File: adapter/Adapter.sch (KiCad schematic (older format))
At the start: 51 parts, among them J1 USB_B_Micro, J2 2040210-1, J3 USB_C_Receptacle, J4 Conn_01x05_Male, J5 Conn_01x03_Male, Q1 IRLML2244TRPBF, SW1 RESET, SW2 BOOT, U1 SN75DP119, U2 AZ1117-3.3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

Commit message: state published at http://strfry.org/lg360vr-schematic.pdf
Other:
- note added: "Design Considerations.\n\nWhat to do with extra lane on DP redriver?\n -> route DP1+- as well, disable lane through EN-Z in software\n-> dont route, save hassle, focus on matching DP0\n\nTerminate extra DP lanes or leave open? \n-> just leave as is, link training should disable them\n\n\nMake use of USB in STM32?-> Break out to pin headers?\n-> maybe, just maybe: connect to device USB, and leave 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"
- note added: "STM32 Q&A:\nDoes the VBAT need to be connected? yes, to VDD\nDo we need special decoupling for AVDD? yes, preferably doucupled with bead.\nTODO: Use reference bead\n\nWhich are the analog pins?\nstm32f072rb.pdf p.33 ff -> PA0-PA7, PB0-1\n\n\n5V Tolerant pins?\n-> PF0-1, PB10-11\nTODO: Make sure LED pins are 5V tolerant\n\n\nHow to do reset? -> can it be left floating / on SWD connector?\n-> pulld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"
- note added: "TODO: Compute Resistors\n"
- note added: "Try to do AUX-Snooping..."
- note removed: "AC coupling on RX side?\n\nWhich type of couple cap?"
- note removed: "Compute Resistors\n"
- note removed: "Design Considerations.\n\nWhat to do with extra lane on DP redriver?\n -> route DP1+- as well, disable lane through EN-Z in software\n-> dont route, save hassle, focus on matching DP0\n\nTerminate extra DP lanes or leave open? \n\n\nMake use of USB in STM32?-> Break out to pin headers?\n-> maybe, just maybe: connect to device USB, and leave floating?\n\n\nConnect CONFIG1/CONFIG2 to microcontrolle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"
- note removed: "STM32 Q&A:\nDoes the VBAT need to be connected? yes, to VDD\nDo we need special decoupling for AVDD? yes, with bead\n\nWhich are the analog pins?\nstm32f072rb.pdf p.33 ff -> PA0-PA7, PB0-1\n\n\n5V Tolerant pins?\n-> PF0-1, PB10-11\n\n\nHow to do reset? -> can it be left floating / on SWD connector?\n\n\nWhat is BOOT0?\n\n\nHow we do programming? -> expose SWD Pins + VDD + RESET\n\nDo PF0/1 have a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"
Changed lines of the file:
@@
 encoding utf-8
 Sheet 1 1
-Title ""
-Date ""
-Rev ""
-Comp ""
-Comment1 ""
+Title "LG360VR Adapter Board"
+Date "2019-02-06"
+Rev "v1"
+Comp "strfry"
+Comment1 "Draft"
 Comment2 ""
 Comment3 ""
@@
 	1    0    0    -1
 $EndComp
-Text Notes -2250 7250 0    50   ~ 0
-STM32 Q&A:\nDoes the VBAT need to be connected? yes, to VDD\nDo we need special decoupling for AVDD? yes, with bead\n\nWhich are the analog pins?\nstm32f072rb.pdf p.33 ff -> PA0-PA7, PB0-1\n\n\n5V Tolerant pins?\n-> PF0-1, PB10-11\n\n\nHow to do reset?  -> can it be left floating / on SWD connector?\n\n\nWhat is BOOT0?\n\n\nHow we do programming? -> expose SWD Pins + VDD + RESET\n\nDo PF0/1 have a special function? -> Yes, the Mhz Quartz\n\nOpt to not populate Crystal? F0x2 is "crystalless USB type"
-Text Notes -3950 4750 0    50   ~ 0
-Design Considerations.\n\nWhat to do with extra lane on DP redriver?\n -> route DP1+- as well, disable lane through EN-Z in software\n-> dont route, save hassle, focus on matching DP0\n\nTerminate extra DP lanes or leave open? \n\n\nMake use of USB in STM32?-> Break out to pin headers?\n-> maybe, just maybe: connect to device USB, and leave floating?\n\n\nConnect CONFIG1/CONFIG2 to microcontroller, just in case? -> Connect CONFIG2 to CEC AF-Pin\n-> CONFIG1/CONFIG2 is not I2C, would need separate conn to AUX: \nhttp://mikesmods.com/mm-wp/wp-content/uploads/2014/03/Commercial_DP2DVI_Adapter.pdf\n\n\nShould USB-C VBUS be FET switchable? Should CC lines be switched as well?\n-> TI Paper says Disconnect FET is needed -> sth. like \nHigh Side PMOS: IRLML2244TRPBF\n\n\nUSB-PD CC PHY?\n\n\nSPI Self Clock!!!\n
+Text Notes -3000 7450 0    50   ~ 0
+STM32 Q&A:\nDoes the VBAT need to be connected? yes, to VDD\nDo we need special decoupling for AVDD? yes, preferably doucupled with bead.\nTODO: Use reference bead\n\nWhich are the analog pins?\nstm32f072rb.pdf p.33 ff -> PA0-PA7, PB0-1\n\n\n5V Tolerant pins?\n-> PF0-1, PB10-11\nTODO: Make sure LED pins are 5V tolerant\n\n\nHow to do reset?  -> can it be left floating / on SWD connector?\n-> pulldown and provide button\n\nWhat is BOOT0?\n-> essentially enables builtin serial bootrom, unless disabled by config register\n\n\nHow we do programming? -> expose SWD Pins + VDD + RESET\n\nDo PF0/1 have a special function? -> Yes, the Mhz Quartz\n\nOpt to not populate Crystal? F0x2 is "crystalless USB type"
+Text Notes -3850 3250 0    50   ~ 0
+Design Considerations.\n\nWhat to do with extra lane on DP redriver?\n -> route DP1+- as well, disable lane through EN-Z in software\n-> dont route, save hassle, focus on matching DP0\n\nTerminate extra DP lanes or leave open? \n-> just leave as is, link training should disable them\n\n\nMake use of USB in STM32?-> Break out to pin headers?\n-> maybe, just maybe: connect to device USB, and leave floating?\n\n\nConnect CONFIG1/CONFIG2 to microcontroller, just in case? -> Connect CONFIG2 to CEC AF-Pin\n-> CONFIG1/CONFIG2 is not I2C, would need separate conn to AUX: \nhttp://mikesmods.com/mm-wp/wp-content/uploads/2014/03/Commercial_DP2DVI_Adapter.pdf\n-> dont bother\n\nShould USB-C VBUS be FET switchable? Should CC lines be switched as well?\n-> TI Paper says Disconnect FET is needed -> sth. like \nHigh Side PMOS: IRLML2244TRPBF\n\n\nUSB-PD CC PHY? -> almost done\nTODO: Correct resistor value for 3.3V\n\n\nSPI Self Clock!!! -> check, TX_CLK\n\n\nAC coupling on RX side? -> yes\n\nWhich type of couple cap?\n-> Intel doc on PCIe recommend 100nF X7R, should be fine
 NoConn ~ 5000 1600
 NoConn ~ 5000 1700
@@
 	1    0    0    -1
 $EndComp
-Text Notes 6750 1100 0    50   ~ 0
-AC coupling on RX side?\n\nWhich type of couple cap?
 $Comp
 L power:VDD #PWR0123
@@
 Discuss best connector type
 Text Notes 850  7550 0    50   ~ 0
-Compute Resistors\n
+TODO: Compute Resistors\n
+Text Notes 4050 6150 0    50   ~ 0
+Try to do AUX-Snooping...
 $EndSCHEMATC

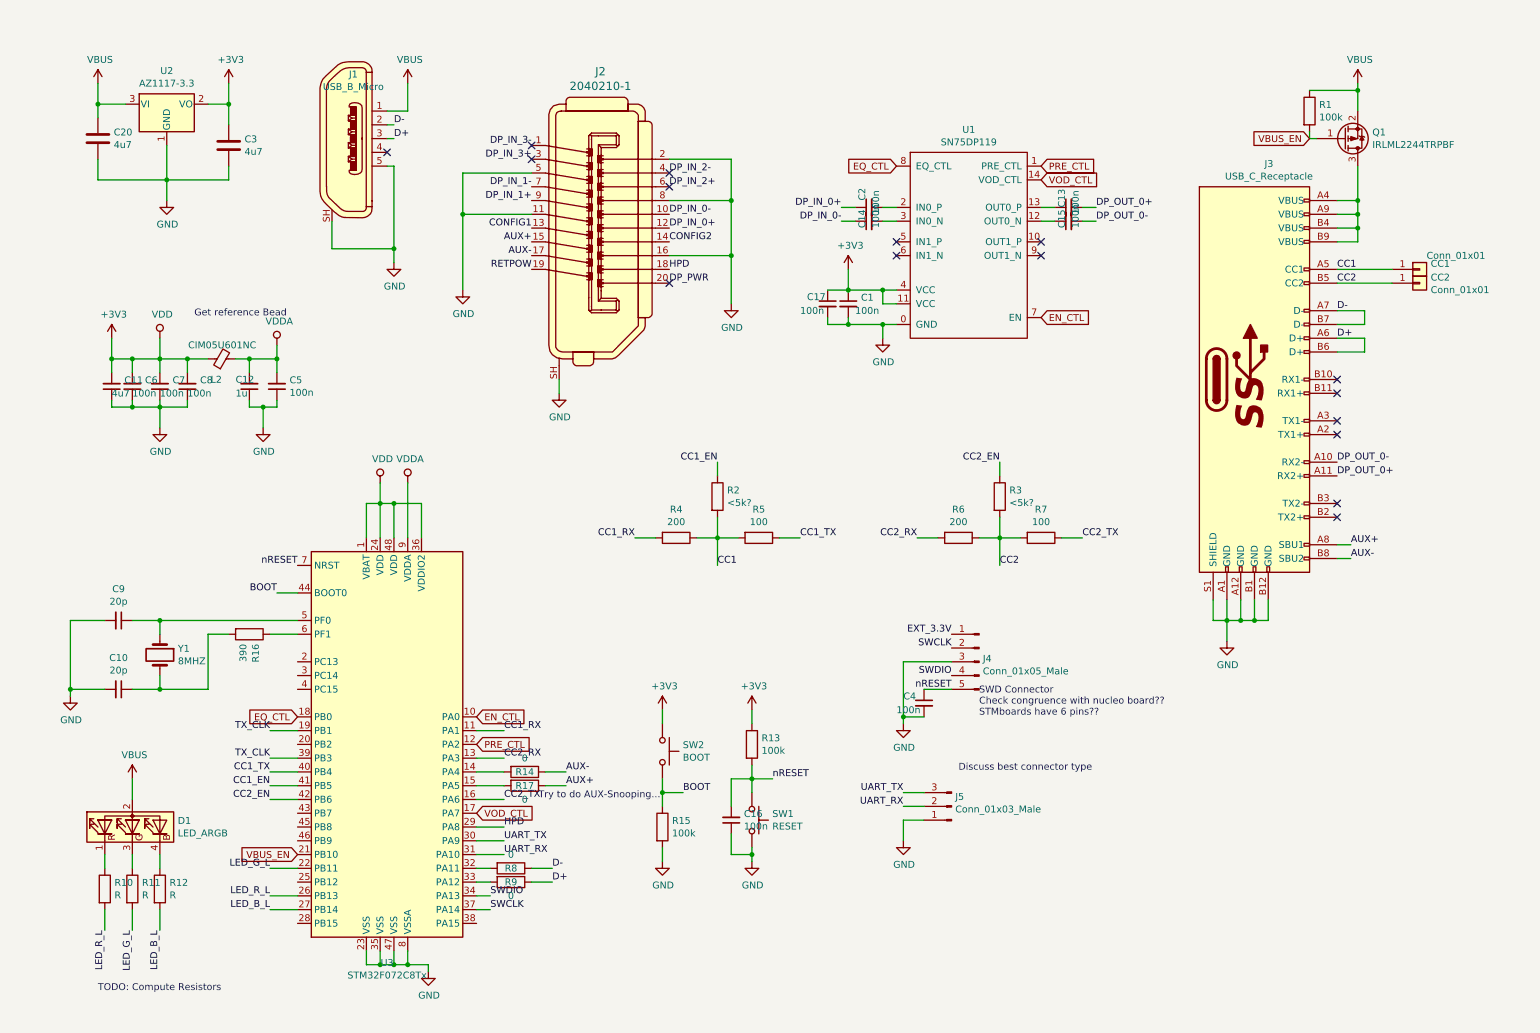
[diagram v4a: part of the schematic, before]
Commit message: Replaced SN75DP119 symbol/footprint with premade one from Arrow librarian
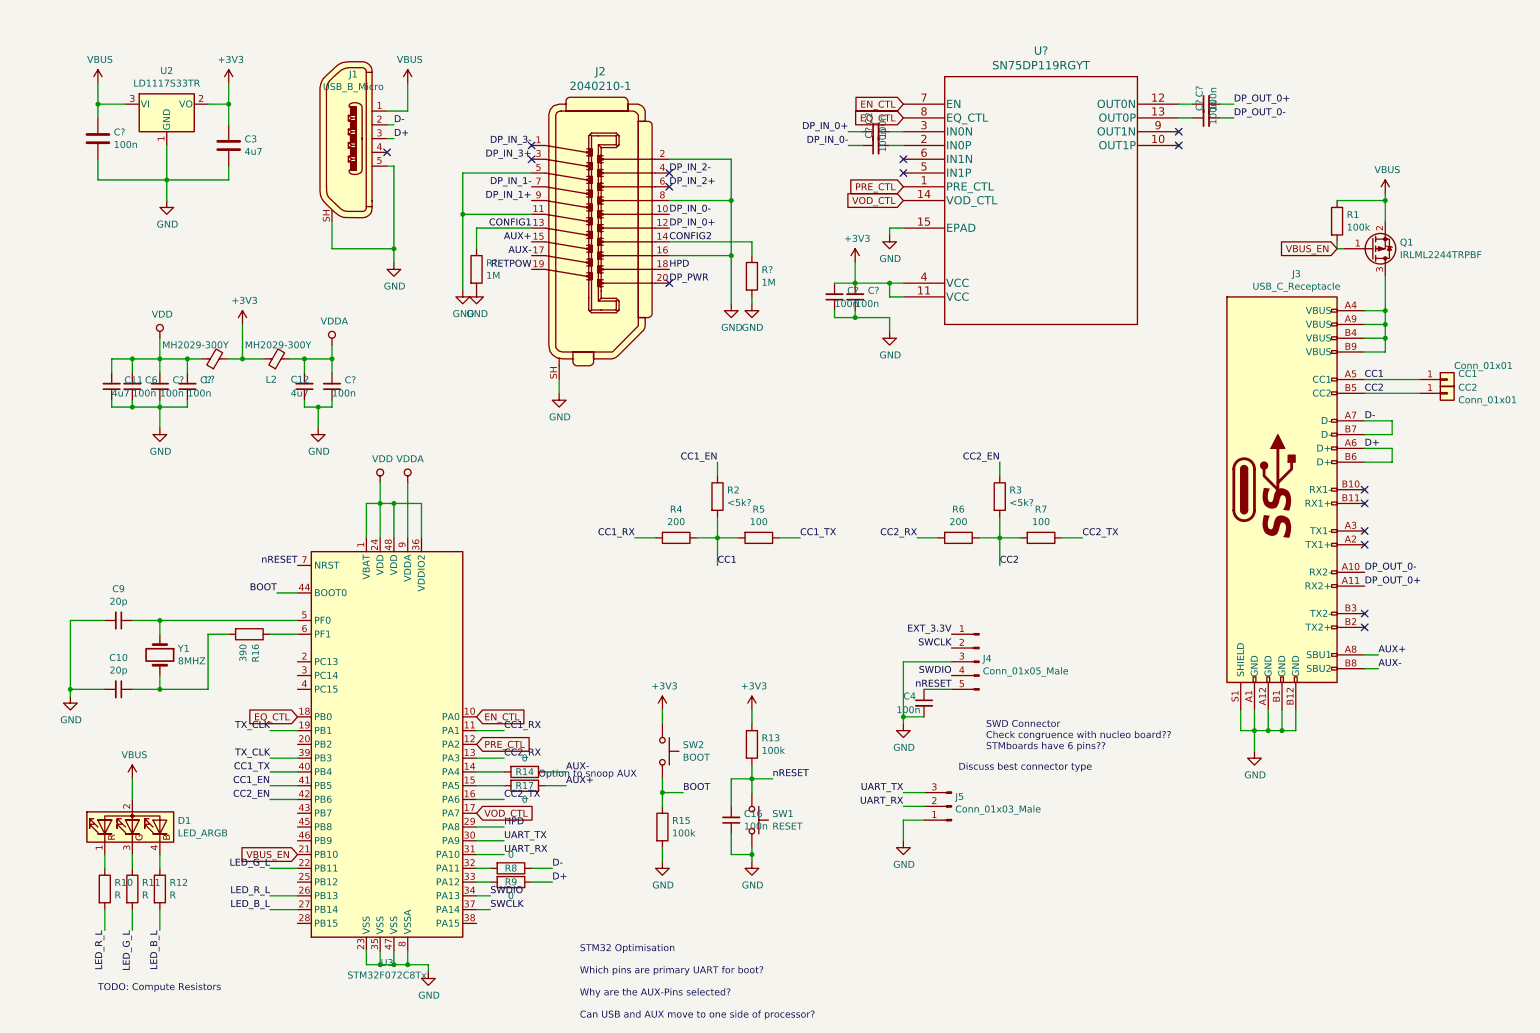
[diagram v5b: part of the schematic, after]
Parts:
- removed C1, C17, C5, C7, C8: 100n, Capacitor_SMD:C_0603_1608Metric_Pad1.05x0.95mm_HandSolder, symbol Device:C_Small
- removed C13, C14, C15: 100n, Capacitor_SMD:C_0402_1005Metric, symbol Device:C_Small
- removed C20: 4u7, Capacitor_SMD:C_0603_1608Metric_Pad1.05x0.95mm_HandSolder, symbol Device:C
- removed U1: SN75DP119, SN75DP119:QFN-20-1EP_4x4mm_P0.5mm_EP2.5x2.5mm, symbol DisplayPort_Redriver:SN75DP119
- added C?: 100n, Capacitor_SMD:C_0603_1608Metric_Pad1.05x0.95mm_HandSolder, symbol Device:C
- added C? (x5): 100n, Capacitor_SMD:C_0603_1608Metric_Pad1.05x0.95mm_HandSolder, symbol Device:C_Small
- added C? (x3): 100n, Capacitor_SMD:C_0402_1005Metric, symbol Device:C_Small
- added L?: MH2029-300Y, Inductor_SMD:L_0805_2012Metric_Pad1.15x1.40mm_HandSolder, symbol Device:Ferrite_Bead_Small
- added R? (x2): 1M, symbol Device:R
- added U?: SN75DP119RGYT, SN75DP119:SN75DP119RGYT, symbol SN75DP119RGYT:SN75DP119RGYT
- C11, C3: S2PN (none) -> CL10A475KO8NNNC
- C12: value 1u -> 4u7; S2PN (none) -> CL10A475KO8NNNC
- C2: S2PN (none) -> CL05J104KP5NNNC
- C6: S2PN (none) -> CL10F104ZO8NNNC
- J1: S2PN (none) -> 10118194-0001LF
- J2: Notes Compatible Molex 47272-0001 -> Compatible Molex 47272-0001 / 47272-0008; S2PN (none) -> 47272-0008
- J3: S2PN (none) -> 12401598E4#2A
- L2: value CIM05U601NC -> MH2029-300Y; footprint Inductor_SMD:L_0603_1608Metric_Pad1.05x0.95mm_HandSolder -> Inductor_SMD:L_0805_2012Metric_Pad1.15x1.40mm_HandSolder; Description (none) -> 30Ohm@100MHz; S2PN (none) -> MH2029-300Y
- Q1: S2PN (none) -> IRLML2244TRPBF
- U2: value AZ1117-3.3 -> LD1117S33TR; MFP AZ1117IH-3.3TRG1 -> LD1117S33TR; S2PN (none) -> LD1117S33TR
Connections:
- net +3V3: now also C?.2, C?.2, L?.2, U?.11 (VCC), U?.4 (VCC); no longer C11.2, C6.2, U3.1 (VBAT), U3.24 (VDD), U3.36 (VDDIO2), U3.48 (VDD)
- net CONFIG1: now also R?.1
- net CONFIG2: now also R?.1
- net DP_IN_0-: now also C?.1
- net DP_OUT_0+: now also C?.2
- net DP_OUT_0-: now also C?.2
- net EN_CTL: now also U?.7 (EN)
- net EQ_CTL: now also U?.8 (EQ_CTL)
- net GND: now also C?.1, C?.1, C?.1, C?.1, C?.1, C?.2, R?.2, R?.2, U?.15 (EPAD)
- net PRE_CTL: now also U?.1 (PRE_CTL)
- net VBUS: now also C?.1
- net VDDA: now also C?.2
- net VOD_CTL: now also U?.14 (VOD_CTL)
- net at C2.2: now also U?.3 (IN0N)
- new net: C?.2, U?.2 (IN0P)
- new net: C?.1, U?.12 (OUT0N)
- new net: C?.1, U?.13 (OUT0P)
- new net VDD: C11.2, C6.2, C?.2, C?.2, L?.1, U3.1 (VBAT), U3.24 (VDD), U3.36 (VDDIO2), U3.48 (VDD)
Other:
- note added: "Option to snoop AUX"
- note added: "STM32 Optimisation\n\nWhich pins are primary UART for boot?\n\nWhy are the AUX-Pins selected?\n\nCan USB and AUX move to one side of processor?"
- note removed: "Get reference Bead"
- note removed: "Try to do AUX-Snooping..."
- moved on the sheet: C12, C2, CC1, CC2, J3, L2, Q1, R1
